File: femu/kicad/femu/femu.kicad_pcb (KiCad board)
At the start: 6 copper layers, 13 x 9.4 mm, 43 parts, among them U1 ESP32-D2WD, U2 FT231XQ, U3 LDO, Y1 ECS-TXO-2016-33-400-TR

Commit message: Adjusting VDD layer to have copper fill (3V3)
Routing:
- added copper zone on In4.Cu, net +3V3
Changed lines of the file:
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@@
+    )
+  )
+  (zone (net 44) (net_name "+3V3") (layer "In4.Cu") (hatch full 0.508)
+    (connect_pads yes (clearance 0.2))
+    (min_thickness 0.127) (filled_areas_thickness no)
+    (fill yes (thermal_gap 0.508) (thermal_bridge_width 0.508))
+    (polygon
+      (pts
+        (xy 135.2042 96.9518)
+        (xy 139.147601 96.941693)
+        (xy 139.1348 92.135908)
+        (xy 140.119189 92.1512)
+        (xy 140.1572 96.9518)
+        (xy 140.1572 101.6762)
+        (xy 127 101.6762)
+        (xy 127 92.1258)
+        (xy 135.2042 92.1258)
+      )
     )
   )

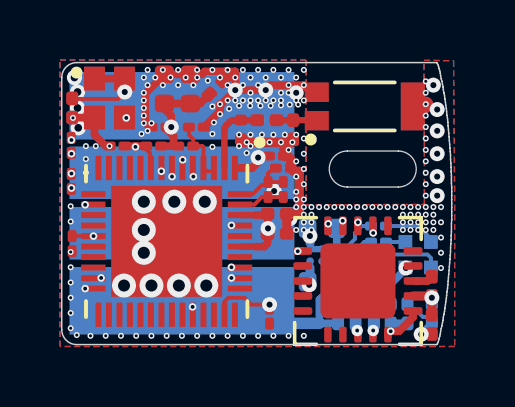
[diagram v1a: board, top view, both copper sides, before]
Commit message: Adjusting RF trace before matching components to be 35ohm impedance. Adjusting tiny RF trace after matching components to be 50ohm impedance
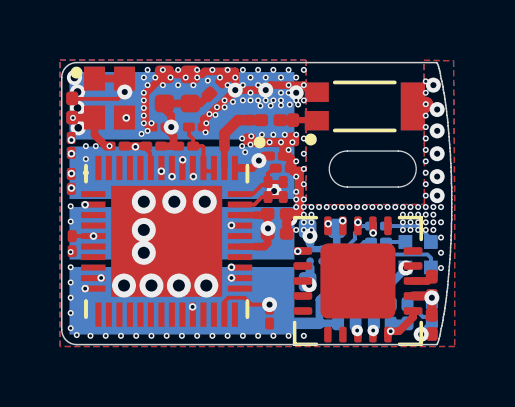
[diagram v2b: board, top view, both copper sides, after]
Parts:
- moved L1 0.28 mm to (133.3, 94.4)
- moved C3 0.13 mm to (134.0, 94.1)
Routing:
- net GND: track 36.4 -> 36.1 mm, vias 197 -> 193
